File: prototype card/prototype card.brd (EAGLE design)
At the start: 100 x 80 mm, 21 parts, among them J1 09231486921, J2 TBP02R1-381-14BE

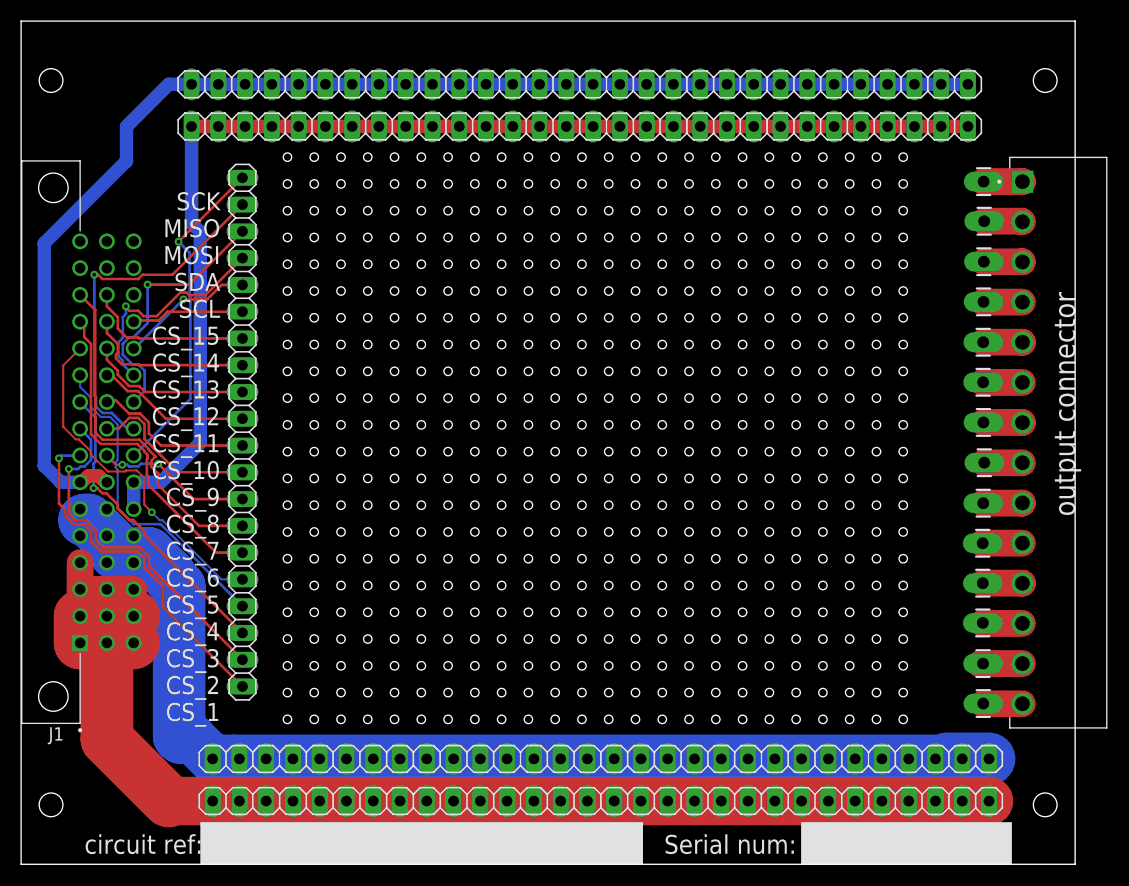
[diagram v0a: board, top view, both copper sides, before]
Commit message: changed pinouts for the boards, next I have to make accomodations for new pinouts and the USB selector system
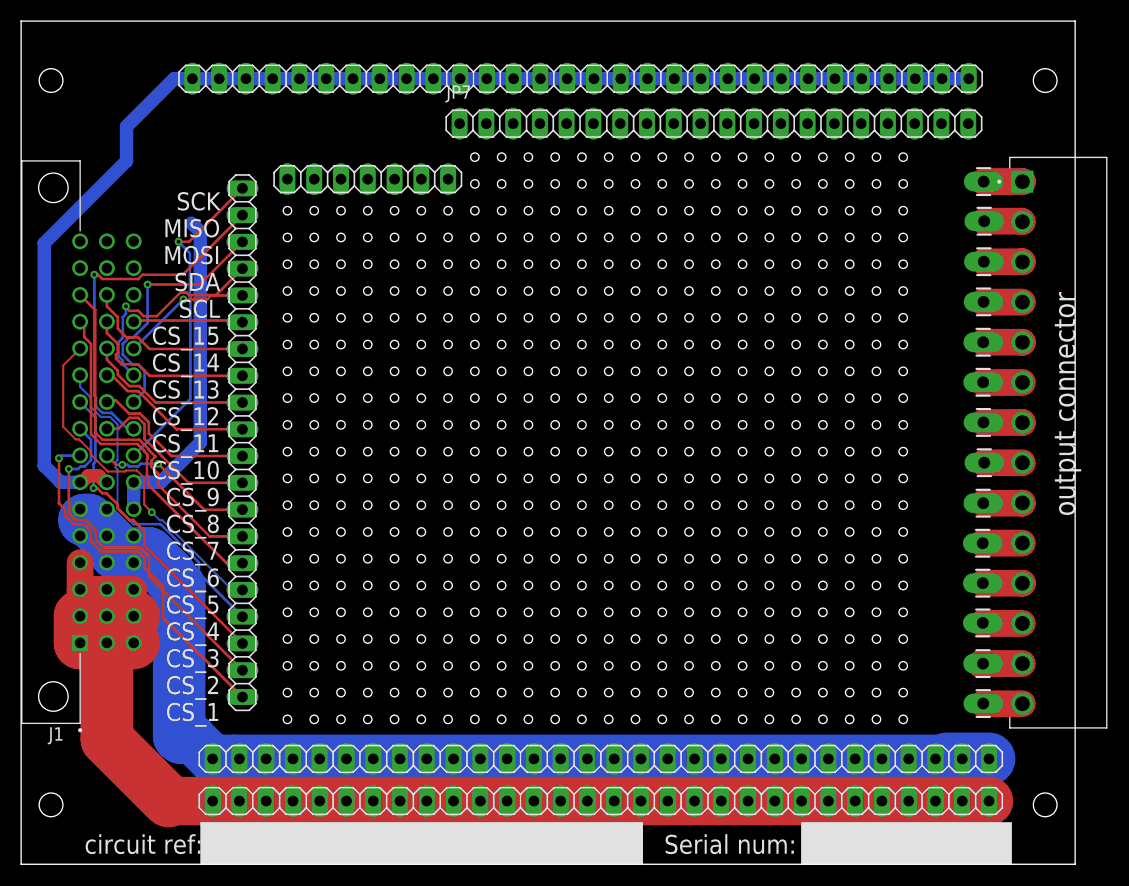
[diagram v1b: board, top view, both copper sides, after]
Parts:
- removed JP4: (no value), pinhead:1X30
- added JP6: (no value), pinhead:1X07
- added JP7: (no value), pinhead:1X20
- moved JP1 1.00 mm to (21.0, 40.0)
- moved JP3 0.54 mm to (53.1, 74.5)
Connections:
- removed net EXT_1: J1.15
- removed net EXT_2: J1.16
- removed net EXT_3: J1.31
- removed net EXT_4: J1.32
- removed net EXT_5: J1.46
- removed net EXT_6: J1.47
- removed net EXT_7: J1.48
- new net RESET: J1.48, JP6.7
- new net USB1_D+: J1.16, JP6.2
- new net USB1_D-: J1.15, JP6.1
- new net USB2_D+: J1.32, JP6.4
- new net USB2_D-: J1.31, JP6.3
- new net USB3_D+: J1.47, JP6.6
- new net USB3_D-: J1.46, JP6.5
- net 5V: now also JP7.1, JP7.10, JP7.11, JP7.12, JP7.13, JP7.14, JP7.15, JP7.16, JP7.17, JP7.18, JP7.19, JP7.2, JP7.20, JP7.3, JP7.4, JP7.5, JP7.6, JP7.7, JP7.8, JP7.9; no longer JP4.1, JP4.10, JP4.11, JP4.12, JP4.13, JP4.14, JP4.15, JP4.16, JP4.17, JP4.18, JP4.19, JP4.2, JP4.20, JP4.21, JP4.22, JP4.23, JP4.24, JP4.25, JP4.26, JP4.27, JP4.28, JP4.29, JP4.3, JP4.30, JP4.4, JP4.5, JP4.6, JP4.7, JP4.8, JP4.9
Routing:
- net 5V: track 188.1 -> 31.6 mm
- net CS_4: track 30.4 -> 31.4 mm
- net CS_3: track 29.1 -> 30.1 mm
- net CS_2: track 33.4 -> 34.4 mm
- net CS_1: track 33.6 -> 34.6 mm

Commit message: made card holes bigger, started usb port work, but I'm not done that part yet
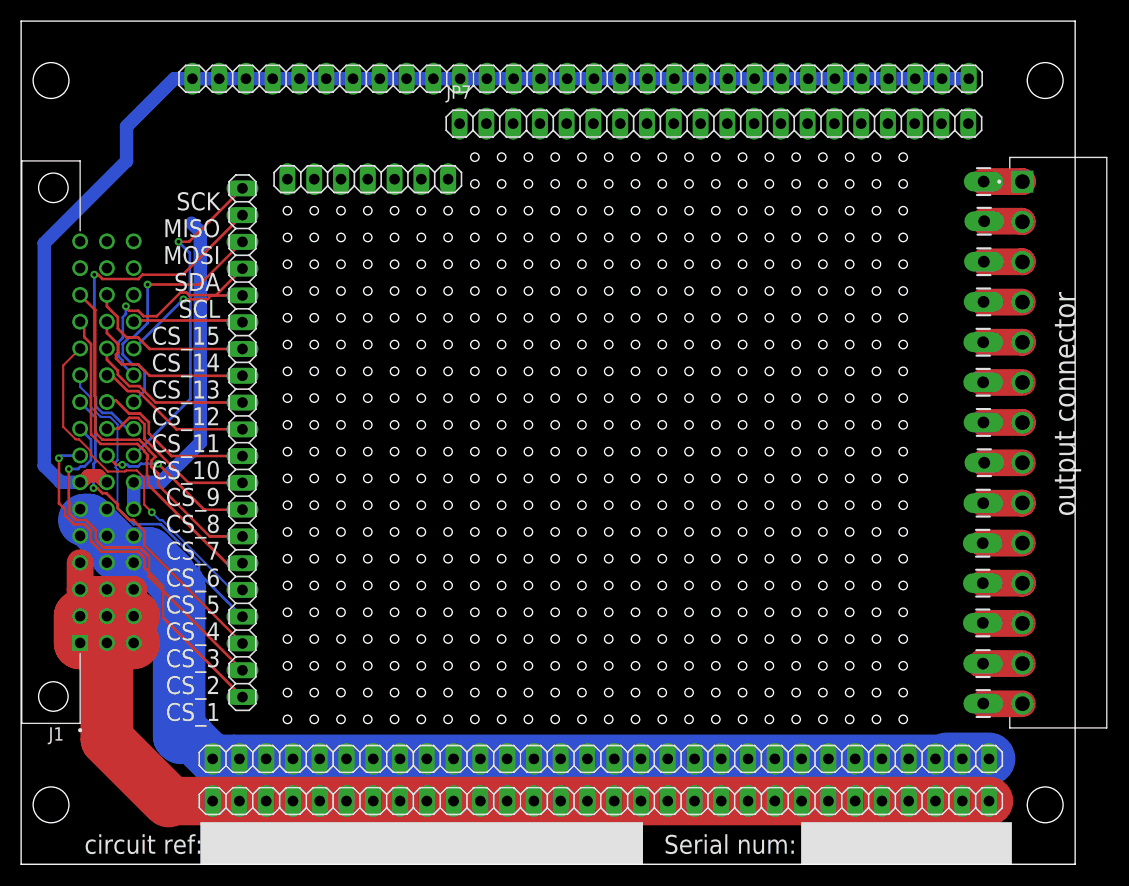
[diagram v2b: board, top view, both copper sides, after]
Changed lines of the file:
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@@
 <wire x1="100" y1="80" x2="0" y2="80" width="0" layer="20"/>
 <wire x1="0" y1="80" x2="0" y2="0" width="0" layer="20"/>
-<hole x="2.84" y="5.64" drill="2.25"/>
-<hole x="2.84" y="74.36" drill="2.25"/>
-<hole x="97.16" y="74.36" drill="2.25"/>
-<hole x="97.16" y="5.64" drill="2.25"/>
+<hole x="2.84" y="5.64" drill="3.4"/>
+<hole x="2.84" y="74.36" drill="3.4"/>
+<hole x="97.16" y="74.36" drill="3.4"/>
+<hole x="97.16" y="5.64" drill="3.4"/>
 <text x="18.9" y="13.6" size="1.7" layer="25" align="bottom-right">SCK
 MISO
@@
 CS_1
 </text>
-<hole x="25.27" y="13.75" drill="0.8" grouprefs="22_PADS PAD"/>
-<rectangle x1="24.27" y1="12.75" x2="26.27" y2="14.75" layer="17" grouprefs="22_PADS PAD"/>
+<hole x="25.27" y="13.75" drill="0.8" grouprefs="PAD 22_PADS"/>
+<rectangle x1="24.27" y1="12.75" x2="26.27" y2="14.75" layer="17" grouprefs="PAD 22_PADS"/>
 <hole x="27.81" y="13.75" drill="0.8" grouprefs="22_PADS"/>
 <hole x="30.35" y="13.75" drill="0.8" grouprefs="22_PADS"/>

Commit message: did some small correction work on the boards
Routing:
- net 5V: track 31.6 -> 120.4 mm, vias 0 -> 2
- net USB3_D-: track 0.00 -> 40.8 mm
- net RESET: track 0.00 -> 39.6 mm, vias 0 -> 1
- net USB3_D+: track 0.00 -> 39.6 mm
- net USB2_D+: track 0.00 -> 37.4 mm, vias 0 -> 2
- net USB1_D+: track 0.00 -> 36.2 mm, vias 0 -> 3
- net USB2_D-: track 0.00 -> 35.2 mm, vias 0 -> 1
- net USB1_D-: track 0.00 -> 32.4 mm, vias 0 -> 1
- net MISO: track 33.8 -> 44.5 mm, vias 1 -> 2
- net MOSI: track 24.6 -> 23.2 mm
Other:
- board text added: "3.3V"
- board text added: "5V"
- board text added: "RST"
- board text added: "USB1_D- USB1_D+ USB2_D- USB2_D+ USB3_D- USB3_D+"
